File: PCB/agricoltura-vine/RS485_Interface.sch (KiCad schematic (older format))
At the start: 22 parts, among them SW2 CVS-02TB, SW3 CVS-02TB, SW4 CVS-02TB, SW5 CVS-02TB, T17 RJHSE-5381, T18 RJHSE-5381, U6 MAX3073EESD+, U7 MAX3073EESD+

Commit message: Route Started Connectors Changed
Changed to QWIIC style connectors and adjusted pinning of RJ45s, but switching to screw terminal header in next commit. THis is a backup
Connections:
- net at R12.1: now also SW2.2; no longer SW2.1
- net at R12.2: now also SW2.1; no longer SW2.2
- net at R14.1: now also SW4.2; no longer SW4.1
- net at R14.2: now also SW4.1; no longer SW4.2
- net at R13.1: now also SW3.2; no longer SW3.1
- net at R13.2: now also SW3.1; no longer SW3.2
- net at R15.1: now also SW5.2; no longer SW5.1
- net at R15.2: now also SW5.1; no longer SW5.2
- new net: SW2.3, T17.6, U6.10 (Z)
- new net: SW4.4, T17.3, U6.11 (B)
- new net: SW4.3, T17.2, U6.12 (A)
- new net: SW2.4, T17.7, U6.9 (Y)
- new net: SW3.3, T18.6, U7.10 (Z)
- new net: SW5.4, T18.3, U7.11 (B)
- new net: SW5.3, T18.2, U7.12 (A)
- new net: SW3.4, T18.7, U7.9 (Y)
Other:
- moved on the sheet: R16, R17, R18, R19, SW2, SW3, SW4, SW5, T17

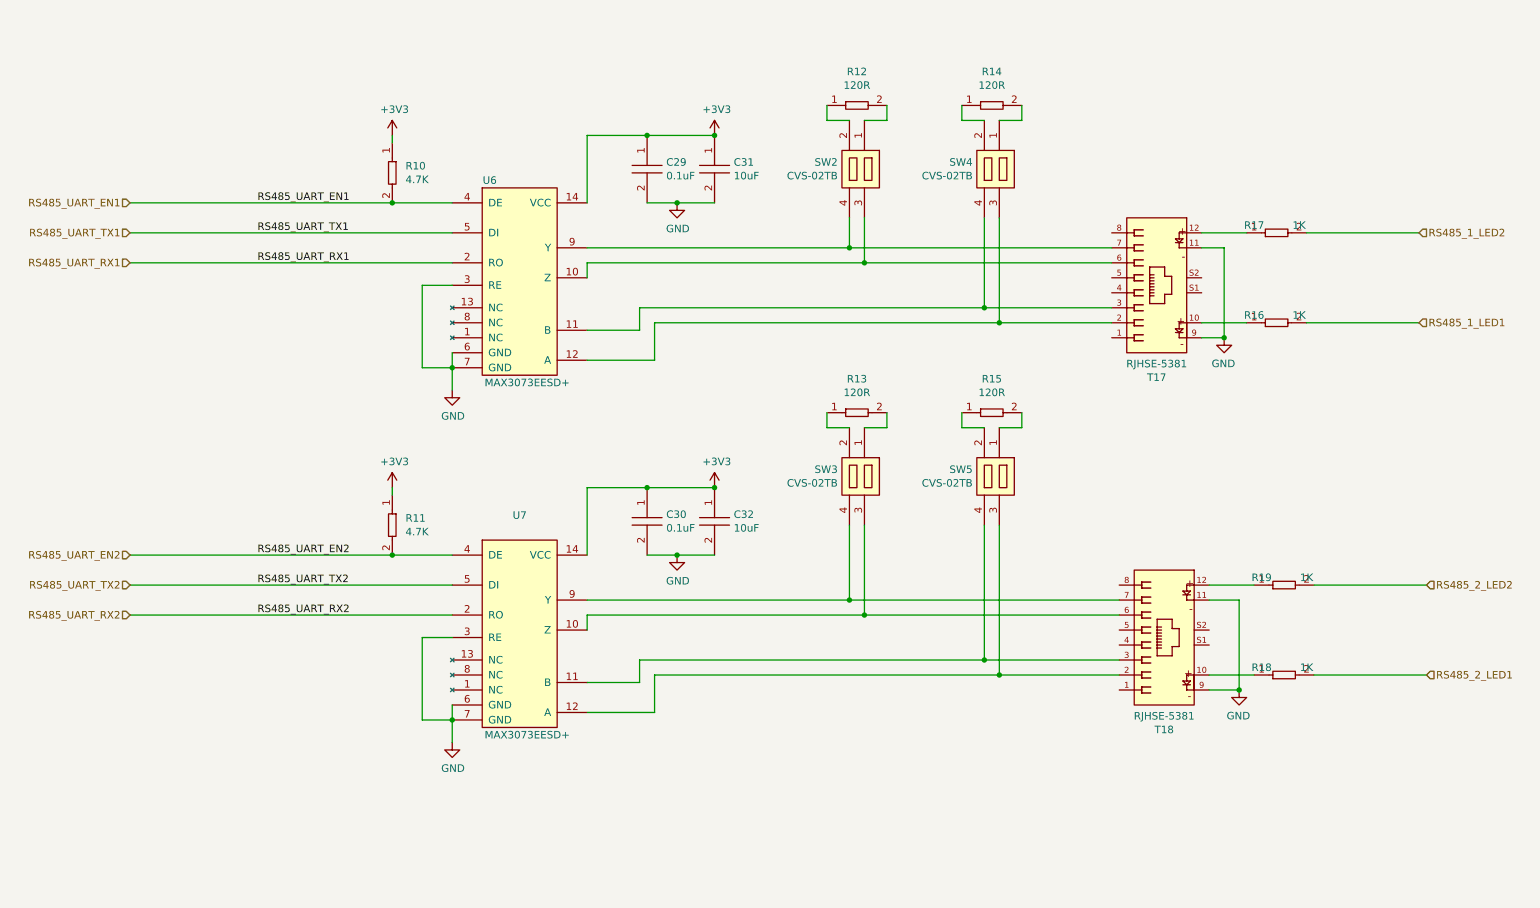
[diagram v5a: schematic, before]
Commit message: Routing and New RS485
swapped over the RS485 chip to a new one and started routing the board.
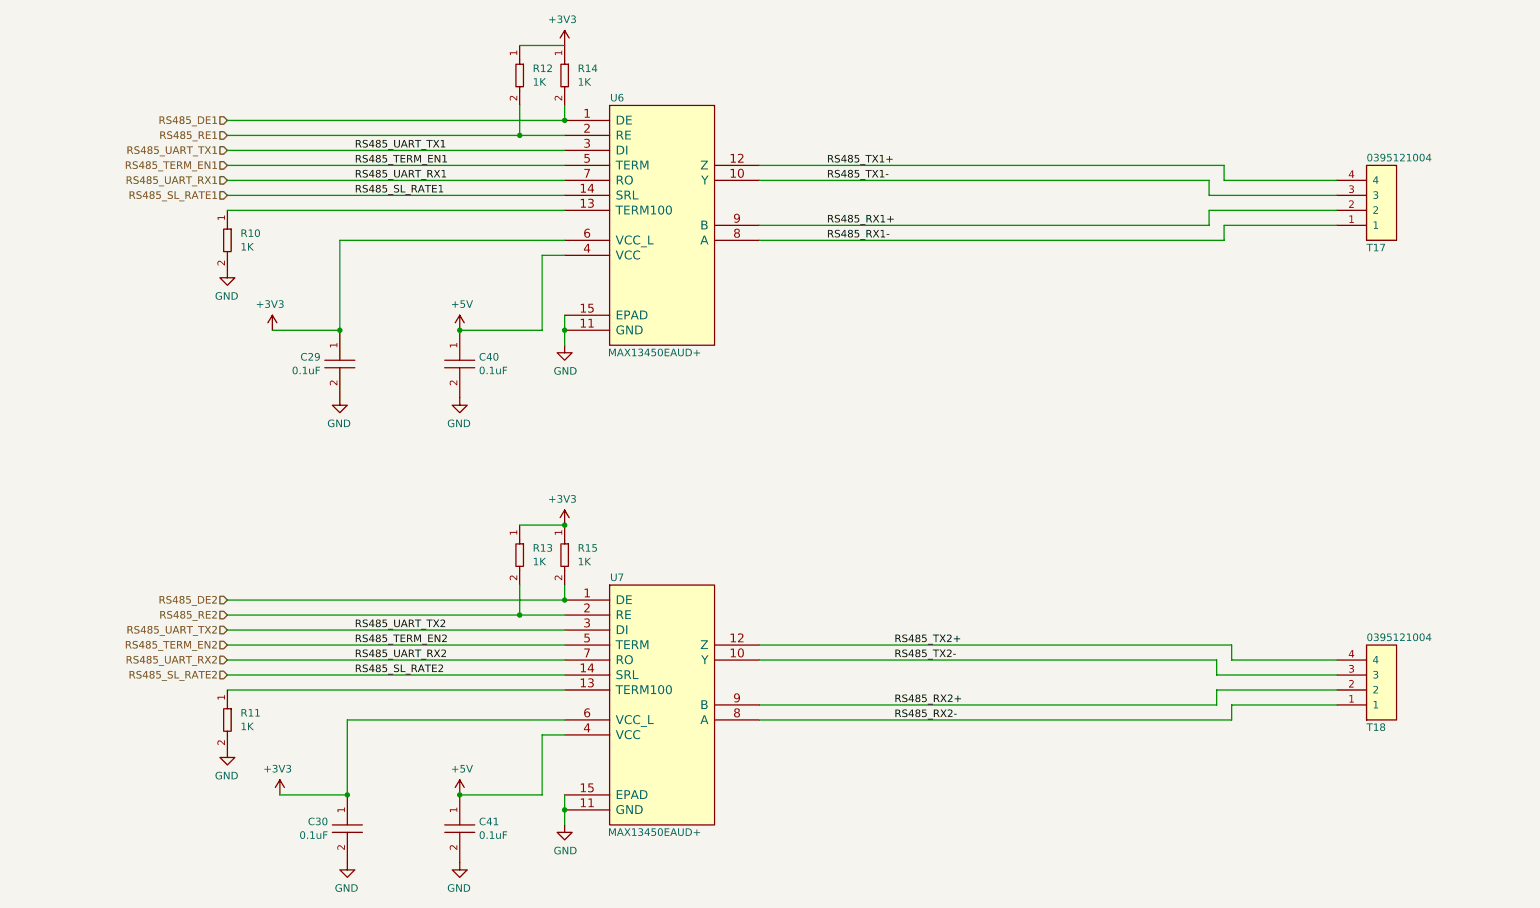
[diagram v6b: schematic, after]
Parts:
- removed C31, C32: GRM188R61A106KE69J, AVR-KiCAD-Lib-Capacitors:C0603, symbol AVR-KiCAD-Lib-Capacitors:GRM188R61A106KE69J
- removed R10, R11: RC0402FR-074K7L, AVR-KiCAD-Lib-Resistors:R0402, symbol AVR-KiCAD-Lib-Resistors:RC0402FR-074K7L
- removed R12, R13, R14, R15: AC0402FR-07120RL, AVR-KiCAD-Lib-Resistors:R0402, symbol AVR-KiCAD-Lib-Resistors:AC0402FR-07120RL
- removed R16, R17, R18, R19: RC0402FR-071KL, AVR-KiCAD-Lib-Resistors:R0402, symbol AVR-KiCAD-Lib-Resistors:RC0402FR-071KL
- removed SW2, SW3, SW4, SW5: CVS-02TB, AVR-KiCAD-Lib-Mech-Switches:CVS-02TB, symbol AVR-KiCAD-Lib-Mech-Switches:CVS-02TB
- removed T17, T18: RJHSE-5381, AVR-KiCAD-Lib-Connectors:AMPHENOL_RJHSE-5381, symbol AVR-KiCAD-Lib-Connectors:RJHSE-5381
- removed U6, U7: MAX3073EESD+, AVR-KiCAD-Lib-ICs:MAX3073EESD&plus_, symbol AVR-KiCAD-Lib-ICs:MAX3073EESD+
- added C40, C41: CGA3E2X7R1H104K080AA, AVR-KiCAD-Lib-Capacitors:C0603, symbol AVR-KiCAD-Lib-Capacitors:CGA3E2X7R1H104K080AA
- added R10, R11, R12, R13, R14, R15: RC0402FR-071KL, AVR-KiCAD-Lib-Resistors:R0402, symbol AVR-KiCAD-Lib-Resistors:RC0402FR-071KL
- added T17, T18: 0395121004, AVR-KiCAD-Lib-Connectors:0395121004, symbol AVR-KiCAD-Lib-Connectors:0395121004
- added U6, U7: MAX13450EAUD+, AVR-KiCAD-Lib-ICs:MAX13450EAUD&plus_, symbol AVR-KiCAD-Lib-ICs:MAX13450EAUD+
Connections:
- net +3V3: now also R12.1, R13.1, R14.1, R15.1, U6.6 (VCC_L), U7.6 (VCC_L)
- net GND: now also C40.2, C41.2, R10.2, R11.2, U6.11 (GND), U6.15 (EPAD), U7.11 (GND), U7.15 (EPAD)
- net RS485_UART_RX1: now also U6.7 (RO)
- net RS485_UART_RX2: now also U7.7 (RO)
- net RS485_UART_TX1: now also U6.3 (DI)
- net RS485_UART_TX2: now also U7.3 (DI)
- new net: R10.1, U6.13 (TERM100)
- new net: R11.1, U7.13 (TERM100)
- new net +5V: C40.1, C41.1, U6.4 (VCC), U7.4 (VCC)
- new net RS485_DE1: R14.2, U6.1 (DE)
- new net RS485_DE2: R15.2, U7.1 (DE)
- new net RS485_RE1: R12.2, U6.2 (RE)
- new net RS485_RE2: R13.2, U7.2 (RE)
- new net RS485_RX1+: T17.2, U6.9 (B)
- new net RS485_RX1-: T17.1, U6.8 (A)
- new net RS485_RX2+: T18.2, U7.9 (B)
- new net RS485_RX2-: T18.1, U7.8 (A)
- new net RS485_SL_RATE1: U6.14 (SRL)
- new net RS485_SL_RATE2: U7.14 (SRL)
- new net RS485_TERM_EN1: U6.5 (TERM)
- new net RS485_TERM_EN2: U7.5 (TERM)
- new net RS485_TX1+: T17.4, U6.12 (Z)
- new net RS485_TX1-: T17.3, U6.10 (Y)
- new net RS485_TX2+: T18.4, U7.12 (Z)
- new net RS485_TX2-: T18.3, U7.10 (Y)
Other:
- moved on the sheet: C29, C30

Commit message: Netlabels and Datasheets
Removed datasheets for parts no longer in design, added datasheet for RS485 transceiver. Added netlabels for RS485 signals.
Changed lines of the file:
@@
 	-1   0    0    -1
 $EndComp
+Text Label 3450 1650 0    50   ~ 0
+RS485_UART_DE1
+Text Label 3450 1750 0    50   ~ 0
+RS485_UART_RE1
+Text Label 3450 4850 0    50   ~ 0
+RS485_UART_DE2
+Text Label 3450 4950 0    50   ~ 0
+RS485_UART_RE2
 $EndSCHEMATC
